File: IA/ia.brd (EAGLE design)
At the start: 90 x 60 mm, 20 parts, among them IC1 7805TV

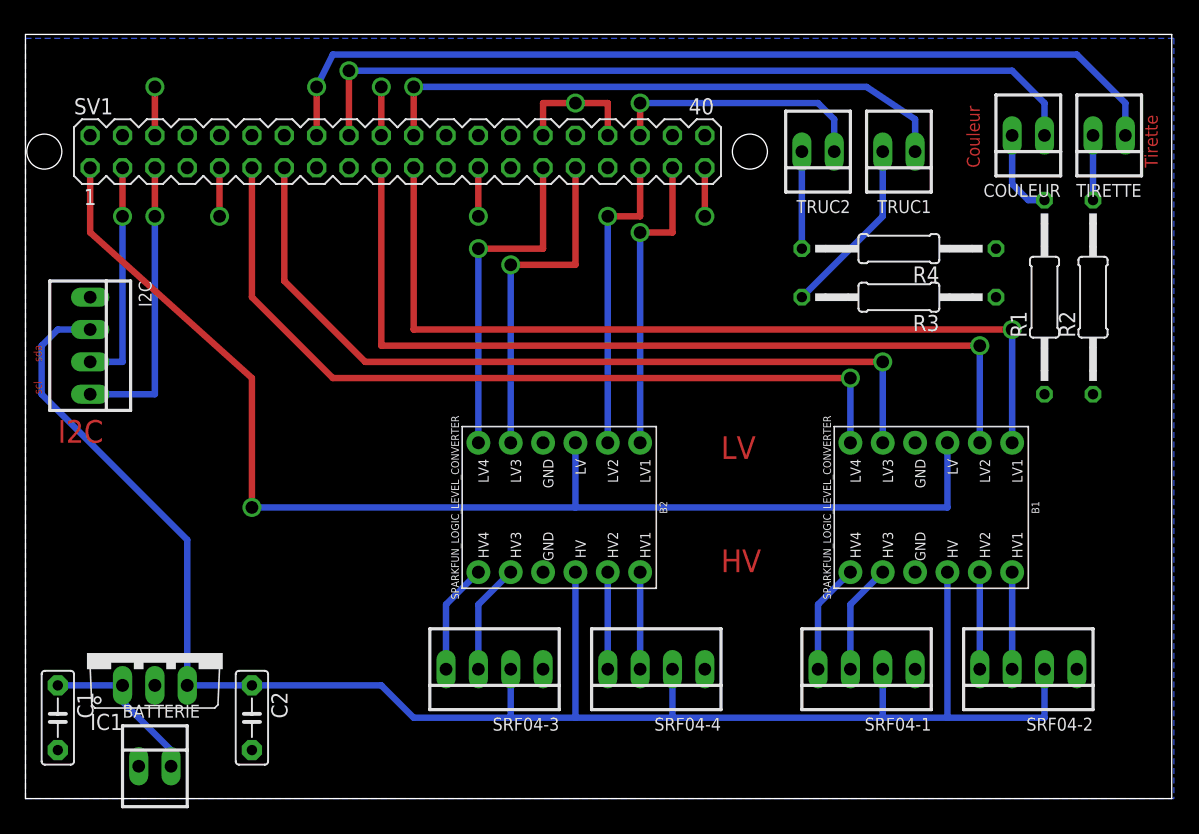
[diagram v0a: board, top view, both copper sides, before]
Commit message: ajout d'un i2c sur l'asserv et design de l'ia
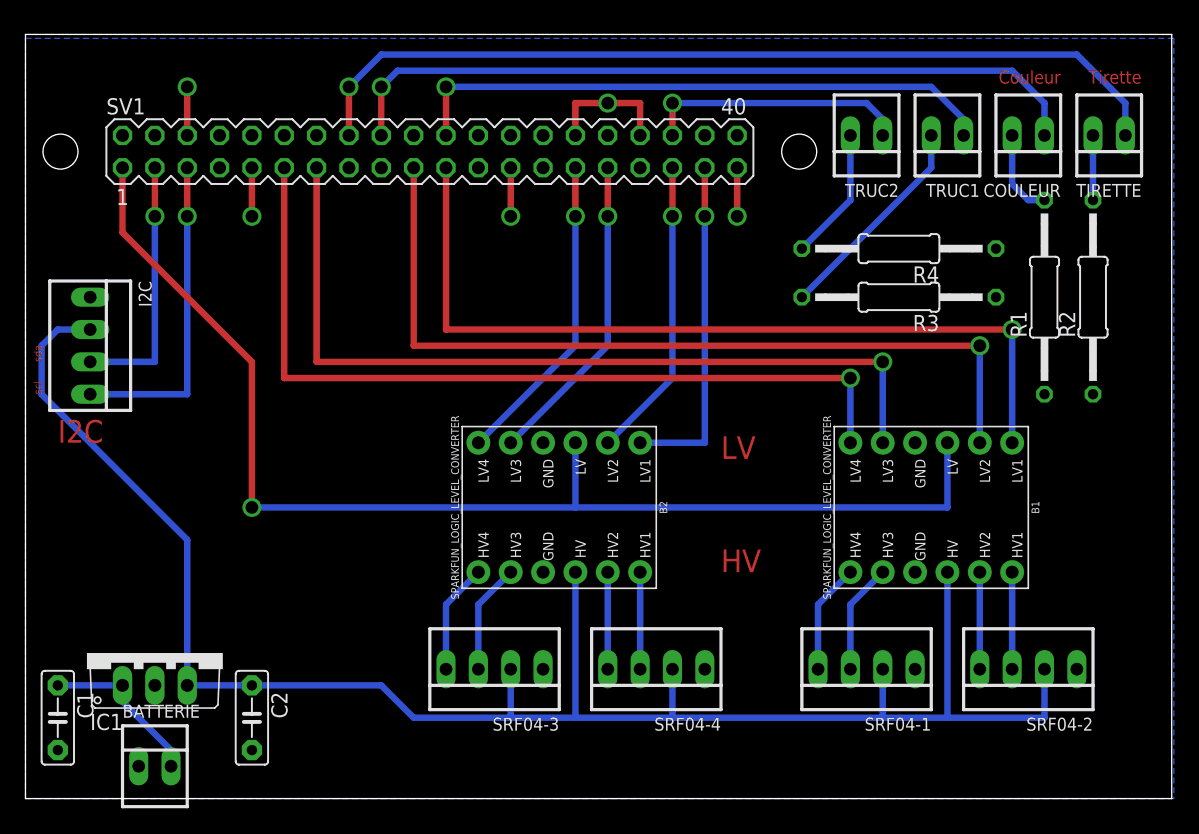
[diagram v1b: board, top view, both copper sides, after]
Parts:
- moved TRUC2 4.02 mm to (66.0, 52.1)
- moved TRUC1 4.02 mm to (72.4, 52.1)
- moved SV1 2.54 mm to (31.8, 50.8)
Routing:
- net GND: track 29.2 -> 25.4 mm, vias 6 -> 5
- net GPIO05: track 63.3 -> 60.0 mm
- net GPIO04: track 73.0 -> 69.9 mm
- net N$12: track 14.1 -> 16.9 mm
- net N$13: track 7.62 -> 10.5 mm
- net GPIO25: track 24.1 -> 26.7 mm
- net GPIO13: track 68.6 -> 66.0 mm
- net GPIO12: track 68.6 -> 66.0 mm
- net SDA: track 17.8 -> 20.3 mm
- net SCL: track 22.9 -> 25.4 mm
- net GPIO22: track 26.7 -> 24.7 mm
- net GPIO21: track 26.7 -> 24.7 mm
- net VCC_1: track 97.1 -> 95.6 mm
- net GPIO02: track 64.9 -> 66.0 mm
- net GPIO00: track 64.9 -> 66.0 mm

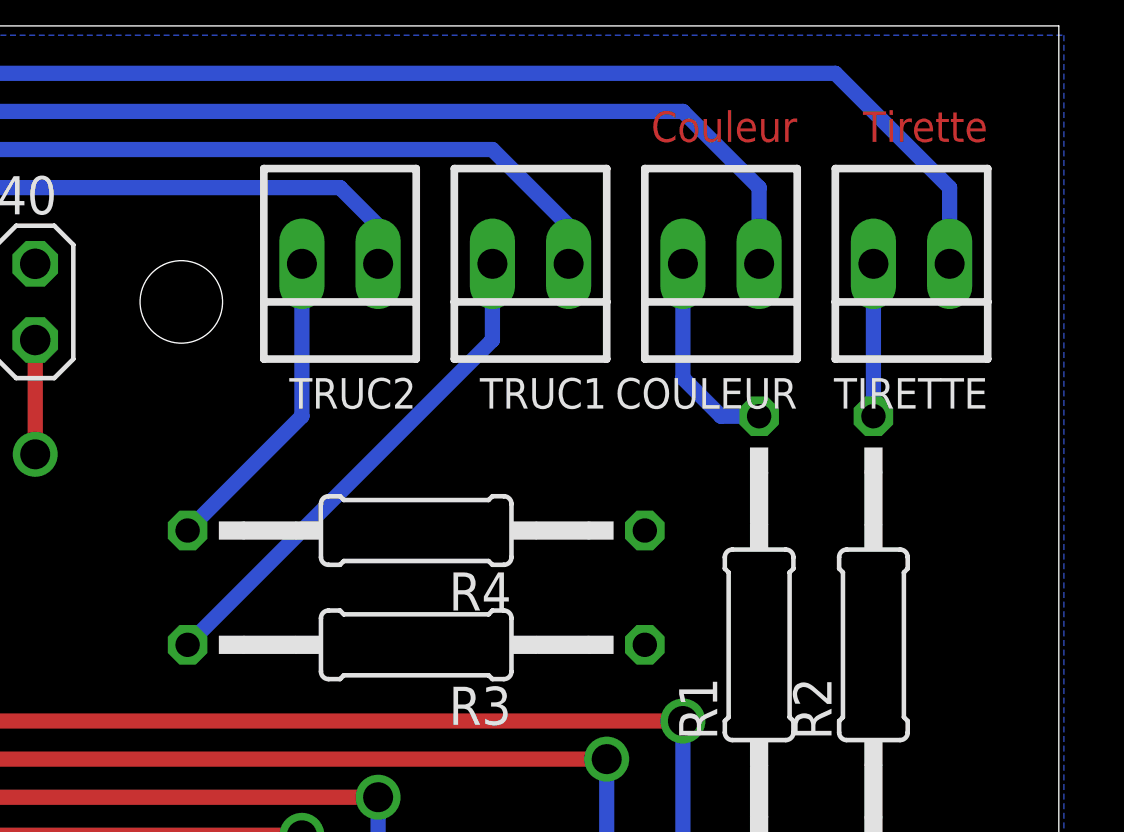
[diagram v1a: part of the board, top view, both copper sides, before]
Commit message: IA: Correction des pullup sur les GPIOs
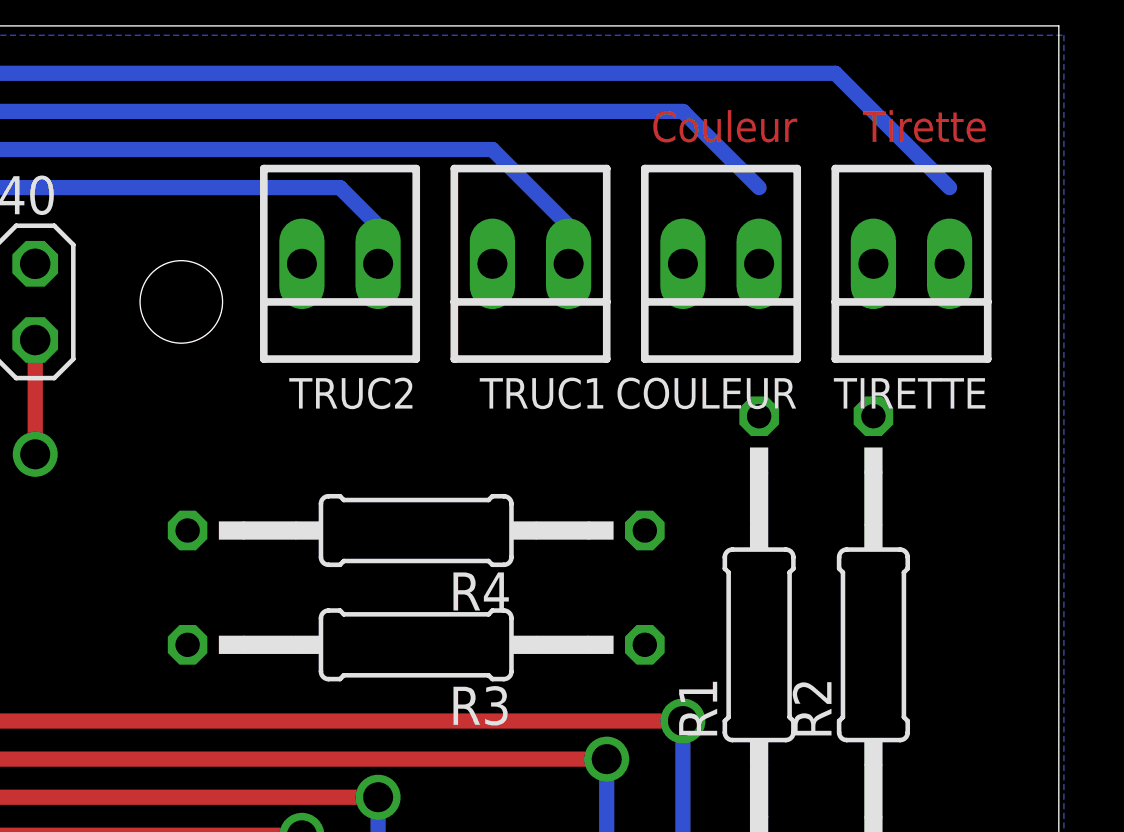
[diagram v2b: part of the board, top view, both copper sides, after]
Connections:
- removed net N$10: R2.2, TIRETTE.2
- removed net N$11: COULEUR.2, R1.2
- removed net N$12: R3.2, TRUC1.2
- removed net N$13: R4.2, TRUC2.2
- net GND: now also COULEUR.2, TIRETTE.2, TRUC1.2, TRUC2.2; no longer R1.1, R2.1, R3.1, R4.1
- net GPIO04: now also R2.2
- net GPIO05: now also R1.2
- net GPIO06: now also R3.2
- net GPIO27: now also R4.2
- net VCC: now also R1.1, R2.1, R3.1, R4.1
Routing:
- net N$12: track 16.9 -> 0.00 mm
- net N$13: track 10.5 -> 0.00 mm
- net N$11: track 6.88 -> 0.00 mm
- net N$10: track 5.08 -> 0.00 mm
- net GPIO05: track 60.0 -> 57.5 mm
- net GPIO04: track 69.9 -> 67.4 mm
- net GPIO27: track 20.8 -> 19.6 mm
- net GPIO06: track 46.8 -> 45.5 mm
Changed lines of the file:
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@@
 <?xml version="1.0" encoding="utf-8"?>
 <!DOCTYPE eagle SYSTEM "eagle.dtd">
-<eagle version="8.6.3">
+<eagle version="8.4.1">
 <drawing>
 <settings>
@@
 <param name="checkRestrict" value="1"/>
 <param name="checkStop" value="0"/>
-<param name="checkValues" value="0"/>
 <param name="useDiameter" value="13"/>
 <param name="maxErrors" value="50"/>
@@
 <contactref element="C2" pad="2"/>
 <contactref element="BATTERIE" pad="1"/>
-<contactref element="R2" pad="1"/>
-<contactref element="R1" pad="1"/>
 <contactref element="SV1" pad="34"/>
 <contactref element="SV1" pad="30"/>
@@
 <contactref element="SV1" pad="25"/>
 <contactref element="SV1" pad="9"/>
-<contactref element="R3" pad="1"/>
-<contactref element="R4" pad="1"/>
 <contactref element="B1" pad="GND2"/>
 <contactref element="B2" pad="GND2"/>
@@
 <wire x1="48.26" y1="54.61" x2="45.72" y2="54.61" width="0.508" layer="1"/>
 <wire x1="17.78" y1="45.72" x2="17.78" y2="49.53" width="0.508" layer="1"/>
+<contactref element="TRUC2" pad="2"/>
+<contactref element="TRUC1" pad="2"/>
+<contactref element="COULEUR" pad="2"/>
+<contactref element="TIRETTE" pad="2"/>
 </signal>
 <signal name="SDA">
@@
 <wire x1="1.27" y1="35.56" x2="2.54" y2="36.83" width="0.508" layer="16"/>
 <wire x1="2.54" y1="36.83" x2="5.08" y2="36.83" width="0.508" layer="16"/>
-</signal>
-<signal name="N$10">
-<contactref element="TIRETTE" pad="2"/>
-<contactref element="R2" pad="2"/>
-<wire x1="83.82" y1="46.99" x2="83.82" y2="52.07" width="0.508" layer="16"/>
-</signal>
-<signal name="N$11">
-<contactref element="COULEUR" pad="2"/>
-<contactref element="R1" pad="2"/>
-<wire x1="80.01" y1="46.99" x2="78.74" y2="46.99" width="0.508" layer="16"/>
-<wire x1="78.74" y1="46.99" x2="77.47" y2="48.26" width="0.508" layer="16"/>
-<wire x1="77.47" y1="48.26" x2="77.47" y2="52.07" width="0.508" layer="16"/>
+<contactref element="R1" pad="1"/>
+<contactref element="R3" pad="1"/>
+<contactref element="R4" pad="1"/>
+<contactref element="R2" pad="1"/>
+<wire x1="76.2" y1="39.37" x2="76.2" y2="43.18" width="0" layer="19" extent="1-1"/>
+<wire x1="80.01" y1="31.75" x2="76.2" y2="39.37" width="0" layer="19" extent="1-1"/>
+<wire x1="83.82" y1="31.75" x2="80.01" y2="31.75" width="0" layer="19" extent="1-1"/>
+<wire x1="72.39" y1="17.78" x2="80.01" y2="31.75" width="0" layer="19" extent="1-1"/>
 </signal>
 <signal name="GPIO05">
-<contactref element="COULEUR" pad="1"/>
 <contactref element="SV1" pad="18"/>
-<wire x1="80.01" y1="52.07" x2="80.01" y2="54.61" width="0.508" layer="16"/>
 <wire x1="80.01" y1="54.61" x2="77.47" y2="57.15" width="0.508" layer="16"/>
 <via x="27.94" y="55.88" extent="1-16" drill="1"/>
@@
 <wire x1="29.21" y1="57.15" x2="27.94" y2="55.88" width="0.508" layer="16"/>
 <wire x1="27.94" y1="52.07" x2="27.94" y2="55.88" width="0.508" layer="1"/>
+<contactref element="COULEUR" pad="1"/>
+<contactref element="R1" pad="2"/>
+<wire x1="80.01" y1="54.61" x2="80.01" y2="52.07" width="0" layer="19" extent="16-16"/>
+<wire x1="80.01" y1="46.99" x2="80.01" y2="52.07" width="0" layer="19" extent="1-1"/>
 </signal>
 <signal name="GPIO04">
-<contactref element="TIRETTE" pad="1"/>
 <contactref element="SV1" pad="16"/>
-<wire x1="86.36" y1="52.07" x2="86.36" y2="54.61" width="0.508" layer="16"/>
 <wire x1="86.36" y1="54.61" x2="82.55" y2="58.42" width="0.508" layer="16"/>
 <via x="25.4" y="55.88" extent="1-16" drill="1"/>
@@
 <wire x1="27.94" y1="58.42" x2="25.4" y2="55.88" width="0.508" layer="16"/>
 <wire x1="25.4" y1="52.07" x2="25.4" y2="55.88" width="0.508" layer="1"/>
-</signal>
-<signal name="N$12">
-<contactref element="TRUC1" pad="2"/>
-<contactref element="R3" pad="2"/>
-<wire x1="60.96" y1="39.37" x2="71.12" y2="49.53" width="0.508" layer="16"/>
-<wire x1="71.12" y1="49.53" x2="71.12" y2="52.07" width="0.508" layer="16"/>
+<contactref element="R2" pad="2"/>
+<contactref element="TIRETTE" pad="1"/>
+<wire x1="86.36" y1="54.61" x2="86.36" y2="52.07" width="0" layer="19" extent="16-16"/>
+<wire x1="83.82" y1="46.99" x2="86.36" y2="52.07" width="0" layer="19" extent="1-1"/>
 </signal>
 <signal name="GPIO06">
-<contactref element="TRUC1" pad="1"/>
 <contactref element="SV1" pad="22"/>
 <via x="33.02" y="55.88" extent="1-16" drill="1"/>
 <wire x1="73.66" y1="53.34" x2="71.12" y2="55.88" width="0.508" layer="16"/>
-<wire x1="73.66" y1="53.34" x2="73.66" y2="52.07" width="0.508" layer="16"/>
 <wire x1="33.02" y1="52.07" x2="33.02" y2="55.88" width="0.508" layer="1"/>
 <wire x1="71.12" y1="55.88" x2="33.02" y2="55.88" width="0.508" layer="16"/>
-</signal>
-<signal name="N$13">
-<contactref element="TRUC2" pad="2"/>
-<contactref element="R4" pad="2"/>
-<wire x1="60.96" y1="43.18" x2="64.77" y2="46.99" width="0.508" layer="16"/>
-<wire x1="64.77" y1="46.99" x2="64.77" y2="52.07" width="0.508" layer="16"/>
+<contactref element="TRUC1" pad="1"/>
+<contactref element="R3" pad="2"/>
+<wire x1="73.66" y1="53.34" x2="73.66" y2="52.07" width="0" layer="19" extent="16-16"/>
+<wire x1="60.96" y1="39.37" x2="73.66" y2="52.07" width="0" layer="19" extent="1-1"/>
 </signal>
 <signal name="GPIO27">
 <contactref element="SV1" pad="36"/>
-<contactref element="TRUC2" pad="1"/>
 <via x="50.8" y="54.61" extent="1-16" drill="1"/>
 <wire x1="66.04" y1="54.61" x2="67.31" y2="53.34" width="0.508" layer="16"/>
-<wire x1="67.31" y1="53.34" x2="67.31" y2="52.07" width="0.508" layer="16"/>
 <wire x1="50.8" y1="52.07" x2="50.8" y2="54.61" width="0.508" layer="1"/>
 <wire x1="50.8" y1="54.61" x2="66.04" y2="54.61" width="0.508" layer="16"/>
+<contactref element="TRUC2" pad="1"/>
+<contactref element="R4" pad="2"/>
+<wire x1="67.31" y1="53.34" x2="67.31" y2="52.07" width="0" layer="19" extent="16-16"/>
+<wire x1="60.96" y1="43.18" x2="67.31" y2="52.07" width="0" layer="19" extent="1-1"/>
 </signal>
 <signal name="N$1">

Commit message: routage IA + gerber
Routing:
- net VCC: track 142.2 -> 177.6 mm
- net GPIO06: track 45.5 -> 65.0 mm
- net GPIO27: track 19.6 -> 32.4 mm
- net GPIO04: track 67.4 -> 76.8 mm
- net GPIO05: track 57.5 -> 65.1 mm
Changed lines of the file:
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@@
 <?xml version="1.0" encoding="utf-8"?>
 <!DOCTYPE eagle SYSTEM "eagle.dtd">
-<eagle version="8.4.1">
+<eagle version="8.6.3">
 <drawing>
 <settings>
@@
 <param name="checkRestrict" value="1"/>
 <param name="checkStop" value="0"/>
+<param name="checkValues" value="0"/>
 <param name="useDiameter" value="13"/>
 <param name="maxErrors" value="50"/>
@@
 <contactref element="R4" pad="1"/>
 <contactref element="R2" pad="1"/>
-<wire x1="76.2" y1="39.37" x2="76.2" y2="43.18" width="0" layer="19" extent="1-1"/>
-<wire x1="80.01" y1="31.75" x2="76.2" y2="39.37" width="0" layer="19" extent="1-1"/>
-<wire x1="83.82" y1="31.75" x2="80.01" y2="31.75" width="0" layer="19" extent="1-1"/>
-<wire x1="72.39" y1="17.78" x2="80.01" y2="31.75" width="0" layer="19" extent="1-1"/>
+<wire x1="76.2" y1="43.18" x2="76.2" y2="39.37" width="0.508" layer="16"/>
+<wire x1="83.82" y1="31.75" x2="80.01" y2="31.75" width="0.508" layer="16"/>
+<wire x1="76.2" y1="39.37" x2="78.74" y2="39.37" width="0.508" layer="16"/>
+<wire x1="78.74" y1="39.37" x2="80.01" y2="38.1" width="0.508" layer="16"/>
+<wire x1="80.01" y1="38.1" x2="80.01" y2="31.75" width="0.508" layer="16"/>
+<wire x1="72.39" y1="17.78" x2="72.39" y2="19.05" width="0.508" layer="16"/>
+<wire x1="80.01" y1="26.67" x2="80.01" y2="31.75" width="0.508" layer="16"/>
+<wire x1="72.39" y1="19.05" x2="80.01" y2="26.67" width="0.508" layer="16"/>
 </signal>
 <signal name="GPIO05">
 <contactref element="SV1" pad="18"/>
-<wire x1="80.01" y1="54.61" x2="77.47" y2="57.15" width="0.508" layer="16"/>
+<wire x1="77.47" y1="57.15" x2="80.01" y2="54.61" width="0.508" layer="16"/>
 <via x="27.94" y="55.88" extent="1-16" drill="1"/>
 <wire x1="77.47" y1="57.15" x2="29.21" y2="57.15" width="0.508" layer="16"/>
@@
 <contactref element="COULEUR" pad="1"/>
 <contactref element="R1" pad="2"/>
-<wire x1="80.01" y1="54.61" x2="80.01" y2="52.07" width="0" layer="19" extent="16-16"/>
-<wire x1="80.01" y1="46.99" x2="80.01" y2="52.07" width="0" layer="19" extent="1-1"/>
+<wire x1="80.01" y1="54.61" x2="80.01" y2="52.07" width="0.508" layer="16"/>
+<wire x1="80.01" y1="52.07" x2="80.01" y2="46.99" width="0.508" layer="16"/>
 </signal>
 <signal name="GPIO04">
 <contactref element="SV1" pad="16"/>
-<wire x1="86.36" y1="54.61" x2="82.55" y2="58.42" width="0.508" layer="16"/>
+<wire x1="82.55" y1="58.42" x2="86.36" y2="54.61" width="0.508" layer="16"/>
 <via x="25.4" y="55.88" extent="1-16" drill="1"/>
 <wire x1="82.55" y1="58.42" x2="27.94" y2="58.42" width="0.508" layer="16"/>
@@
 <contactref element="R2" pad="2"/>
 <contactref element="TIRETTE" pad="1"/>
-<wire x1="86.36" y1="54.61" x2="86.36" y2="52.07" width="0" layer="19" extent="16-16"/>
-<wire x1="83.82" y1="46.99" x2="86.36" y2="52.07" width="0" layer="19" extent="1-1"/>
+<wire x1="86.36" y1="54.61" x2="86.36" y2="52.07" width="0.508" layer="16"/>
+<wire x1="86.36" y1="48.26" x2="85.09" y2="46.99" width="0.508" layer="16"/>
+<wire x1="85.09" y1="46.99" x2="83.82" y2="46.99" width="0.508" layer="16"/>
+<wire x1="86.36" y1="52.07" x2="86.36" y2="48.26" width="0.508" layer="16"/>
 </signal>
 <signal name="GPIO06">
@@
 <contactref element="TRUC1" pad="1"/>
 <contactref element="R3" pad="2"/>
+<wire x1="73.66" y1="52.07" x2="73.66" y2="49.53" width="0.508" layer="16"/>
+<wire x1="73.66" y1="49.53" x2="63.5" y2="39.37" width="0.508" layer="16"/>
+<wire x1="63.5" y1="39.37" x2="60.96" y2="39.37" width="0.508" layer="16"/>
 <wire x1="73.66" y1="53.34" x2="73.66" y2="52.07" width="0" layer="19" extent="16-16"/>
-<wire x1="60.96" y1="39.37" x2="73.66" y2="52.07" width="0" layer="19" extent="1-1"/>
 </signal>
 <signal name="GPIO27">
 <contactref element="SV1" pad="36"/>
 <via x="50.8" y="54.61" extent="1-16" drill="1"/>
-<wire x1="66.04" y1="54.61" x2="67.31" y2="53.34" width="0.508" layer="16"/>
+<wire x1="67.31" y1="53.34" x2="66.04" y2="54.61" width="0.508" layer="16"/>
 <wire x1="50.8" y1="52.07" x2="50.8" y2="54.61" width="0.508" layer="1"/>
 <wire x1="50.8" y1="54.61" x2="66.04" y2="54.61" width="0.508" layer="16"/>
 <contactref element="TRUC2" pad="1"/>
 <contactref element="R4" pad="2"/>
-<wire x1="67.31" y1="53.34" x2="67.31" y2="52.07" width="0" layer="19" extent="16-16"/>
-<wire x1="60.96" y1="43.18" x2="67.31" y2="52.07" width="0" layer="19" extent="1-1"/>
+<wire x1="67.31" y1="52.07" x2="67.31" y2="53.34" width="0.508" layer="16"/>
+<wire x1="67.31" y1="52.07" x2="67.31" y2="50.8" width="0.508" layer="16"/>
+<wire x1="67.31" y1="50.8" x2="60.96" y2="44.45" width="0.508" layer="16"/>
+<wire x1="60.96" y1="44.45" x2="60.96" y2="43.18" width="0.508" layer="16"/>
 </signal>
 <signal name="N$1">
